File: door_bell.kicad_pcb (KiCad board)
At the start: 4 copper layers, 68.6 x 68.6 mm, 77 parts, among them J1 8-10V AC/DC, J2 Speaker, J3 SWITCH1, J4 UART, J5 MicroSD, J6 Door panel, K1 HJR 1-2C, Q1 BC847, SW1 Reset, SW2 Boot, U1 NCP1117-5v, U2 MAX98357A, U3 NCP1117-3v3, U4 DS3231M, U5 MAX3232, U6 ESP32-WROVER-B, U7 74LVC2G14

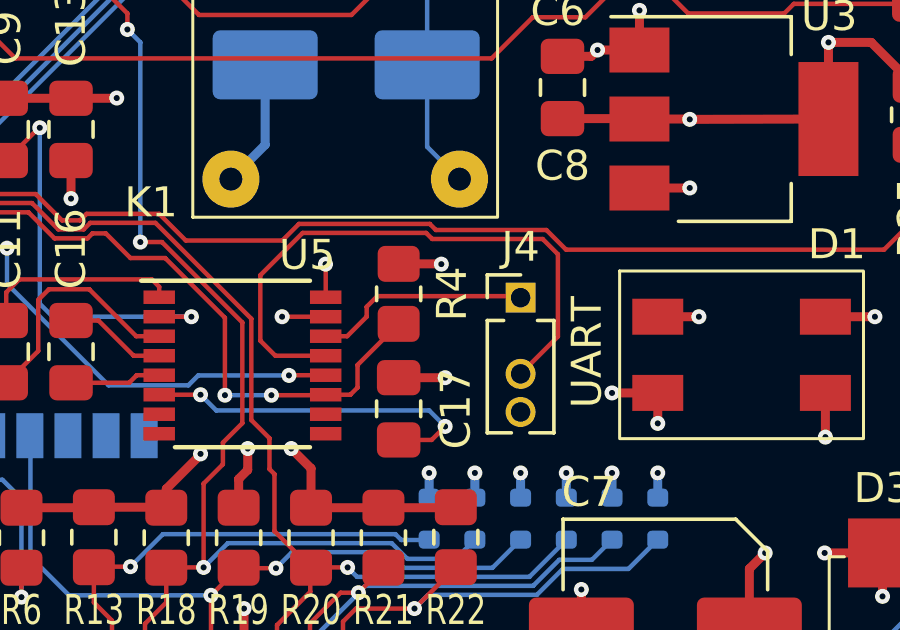
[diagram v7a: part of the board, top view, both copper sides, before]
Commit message: Re-route connections to UART pin header
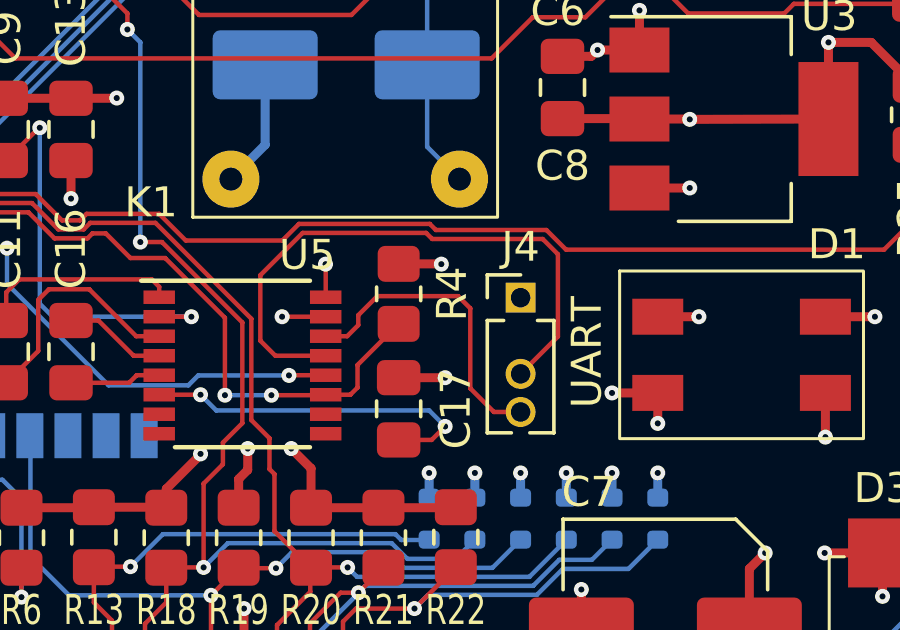
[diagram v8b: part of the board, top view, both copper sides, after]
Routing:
- net GND: track 447.9 -> 452.1 mm
- net Net-(J4-Pin_4): track 7.26 -> 10.4 mm
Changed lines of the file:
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@@
     (attr through_hole)
     (fp_text reference "J4" (at 0 -1.695) (layer "F.SilkS")
-        (effects (font (size 1 1) (thickness 0.15)))
+        (effects (font (size 1 1) (thickness 0.153)))
     )
     (fp_text value "UART" (at 0 5.505) (layer "F.Fab")
@@
   (segment (start 112.4204 92.9132) (end 112.4204 86.5886) (width 0.3) (layer "In1.Cu") (net 1))
   (segment (start 120.7516 91.9988) (end 120.7516 90.7288) (width 0.3) (layer "In1.Cu") (net 1))
+  (segment (start 150.876 91.059) (end 147.828 91.059) (width 0.3) (layer "In1.Cu") (net 1))
   (segment (start 126.1618 65.024) (end 126.1618 64.4906) (width 0.3) (layer "In1.Cu") (net 1))
   (segment (start 160.147 106.9594) (end 149.86 106.9594) (width 0.3) (layer "In1.Cu") (net 1))
@@
   (segment (start 130.2004 80.137) (end 130.2004 74.4982) (width 0.3) (layer "In1.Cu") (net 1))
   (segment (start 133.2738 106.807) (end 131.318 106.807) (width 0.3) (layer "In1.Cu") (net 1))
+  (segment (start 150.876 94.234) (end 150.876 91.059) (width 0.3) (layer "In1.Cu") (net 1))
   (segment (start 127.1016 103.886) (end 127.1016 106.7054) (width 0.3) (layer "In1.Cu") (net 1))
   (segment (start 131.318 112.649) (end 129.286 112.649) (width 0.3) (layer "In1.Cu") (net 1))
@@
   (segment (start 131.318 117.4496) (end 131.318 117.856) (width 0.3) (layer "In1.Cu") (net 1))
   (segment (start 120.7516 90.7288) (end 120.7516 88.4682) (width 0.3) (layer "In1.Cu") (net 1))
-  (segment (start 147.828 96.901) (end 147.828 94.869) (width 0.3) (layer "In1.Cu") (net 1))
   (segment (start 158.0642 67.437) (end 158.0642 66.167) (width 0.3) (layer "In1.Cu") (net 1))
   (segment (start 120.7516 90.7288) (end 118.1608 90.7288) (width 0.3) (layer "In1.Cu") (net 1))
@@
   (segment (start 128.93 72.212601) (end 128.93 77.88) (width 0.15) (layer "B.Cu") (net 48))
   (segment (start 128.9304 72.212201) (end 128.93 72.212601) (width 0.15) (layer "B.Cu") (net 48))
-  (segment (start 143.0528 91.0082) (end 147.7772 91.0082) (width 0.15) (layer "F.Cu") (net 49))
-  (segment (start 147.7772 91.0082) (end 147.828 91.059) (width 0.15) (layer "F.Cu") (net 49))
-  (segment (start 142.6972 91.3638) (end 143.0528 91.0082) (width 0.15) (layer "F.Cu") (net 49))
+  (segment (start 142.4178 91.6432) (end 143.0528 91.0082) (width 0.15) (layer "F.Cu") (net 49))
+  (segment (start 146.1516 91.4146) (end 146.1516 94.0816) (width 0.15) (layer "F.Cu") (net 49))
+  (segment (start 142.4178 91.9734) (end 142.4178 91.6432) (width 0.15) (layer "F.Cu") (net 49))
+  (segment (start 142.0472 92.344) (end 142.4178 91.9734) (width 0.15) (layer "F.Cu") (net 49))
+  (segment (start 146.1516 94.0816) (end 146.939 94.869) (width 0.15) (layer "F.Cu") (net 49))
+  (segment (start 146.939 94.869) (end 147.828 94.869) (width 0.15) (layer "F.Cu") (net 49))
+  (segment (start 143.0528 91.0082) (end 145.7452 91.0082) (width 0.15) (layer "F.Cu") (net 49))
+  (segment (start 145.7452 91.0082) (end 146.1516 91.4146) (width 0.15) (layer "F.Cu") (net 49))
   (segment (start 141.332 92.344) (end 142.0472 92.344) (width 0.15) (layer "F.Cu") (net 49))
-  (segment (start 142.6972 91.694) (end 142.6972 91.3638) (width 0.15) (layer "F.Cu") (net 49))
-  (segment (start 142.0472 92.344) (end 142.6972 91.694) (width 0.15) (layer "F.Cu") (net 49))
   (segment (start 123.8504 112.5474) (end 125.0884 112.5474) (width 0.15) (layer "F.Cu") (net 50))
   (segment (start 122.9614 113.4364) (end 123.8504 112.5474) (width 0.15) (layer "F.Cu") (net 50))
